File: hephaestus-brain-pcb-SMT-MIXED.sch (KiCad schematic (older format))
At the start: 32 parts, among them IC1 ATSAMD51G19A-MU, J1 Barrel_Jack, J2 Conn_02x03_Odd_Even, J3 USB_B_Micro, J4 Conn_02x10_Odd_Even, J5 Conn_01x03_Male, J6 Conn_01x03_Male, J7 Conn_01x03_Male, SW1 SW_SPDT, SW2 SW_SPST, SW3 SW_SPST, U1 LM1117-5.0, U2 AP2112K-3.3, U3 AT25xxx-MA, U4 74LVC1G125

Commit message: Mixed SMT-PTH version.
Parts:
- J1: footprint unified:DC-005-5A-2.0-SMT -> Connector_BarrelJack:BarrelJack_CUI_PJ-102AH_Horizontal
- J2: footprint Connector_PinSocket_2.54mm:PinSocket_2x03_P2.54mm_Vertical_SMD -> Connector_PinSocket_2.54mm:PinSocket_2x03_P2.54mm_Vertical
- J5, J6, J7: footprint Connector_JST:JST_PH_B3B-PH-SM4-TB_1x03-1MP_P2.00mm_Vertical -> Connector_JST:JST_PH_B3B-PH-K_1x03_P2.00mm_Vertical
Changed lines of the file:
@@
 F 0 "J5" H 4922 4082 50  0000 R CNN
 F 1 "Conn_01x03_Male" H 4922 4173 50  0000 R CNN
-F 2 "Connector_JST:JST_PH_B3B-PH-SM4-TB_1x03-1MP_P2.00mm_Vertical" H 4950 4150 50  0001 C CNN
+F 2 "Connector_JST:JST_PH_B3B-PH-K_1x03_P2.00mm_Vertical" H 4950 4150 50  0001 C CNN
 F 3 "B3B-PH-K-S(LF)(SN)" H 4950 4150 50  0001 C CNN
 	1    4950 4150
@@
 F 0 "J1" H 1457 1975 50  0000 C CNN
 F 1 "Barrel_Jack" H 1457 1884 50  0000 C CNN
-F 2 "unified:DC-005-5A-2.0-SMT" H 1450 1610 50  0001 C CNN
+F 2 "Connector_BarrelJack:BarrelJack_CUI_PJ-102AH_Horizontal" H 1450 1610 50  0001 C CNN
 F 3 "PJ-102AH" H 1450 1610 50  0001 C CNN
 F 4 "DC-005-5A-2.0-SMT" H 1400 1650 50  0001 C CNN "mpn"
@@
 F 0 "J6" H 4922 4432 50  0000 R CNN
 F 1 "Conn_01x03_Male" H 4922 4523 50  0000 R CNN
-F 2 "Connector_JST:JST_PH_B3B-PH-SM4-TB_1x03-1MP_P2.00mm_Vertical" H 4950 4500 50  0001 C CNN
+F 2 "Connector_JST:JST_PH_B3B-PH-K_1x03_P2.00mm_Vertical" H 4950 4500 50  0001 C CNN
 F 3 "B3B-PH-K-S(LF)(SN)" H 4950 4500 50  0001 C CNN
 	1    4950 4500
@@
 F 0 "J7" H 4922 4782 50  0000 R CNN
 F 1 "Conn_01x03_Male" H 4922 4873 50  0000 R CNN
-F 2 "Connector_JST:JST_PH_B3B-PH-SM4-TB_1x03-1MP_P2.00mm_Vertical" H 4950 4850 50  0001 C CNN
+F 2 "Connector_JST:JST_PH_B3B-PH-K_1x03_P2.00mm_Vertical" H 4950 4850 50  0001 C CNN
 F 3 "B3B-PH-K-S(LF)(SN)" H 4950 4850 50  0001 C CNN
 	1    4950 4850
@@
 F 0 "J2" H 5350 3417 50  0000 C CNN
 F 1 "Conn_02x03_Odd_Even" H 5350 3326 50  0000 C CNN
-F 2 "Connector_PinSocket_2.54mm:PinSocket_2x03_P2.54mm_Vertical_SMD" H 5300 3100 50  0001 C CNN
+F 2 "Connector_PinSocket_2.54mm:PinSocket_2x03_P2.54mm_Vertical" H 5300 3100 50  0001 C CNN
 F 3 "~" H 5300 3100 50  0001 C CNN
 	1    5300 3100

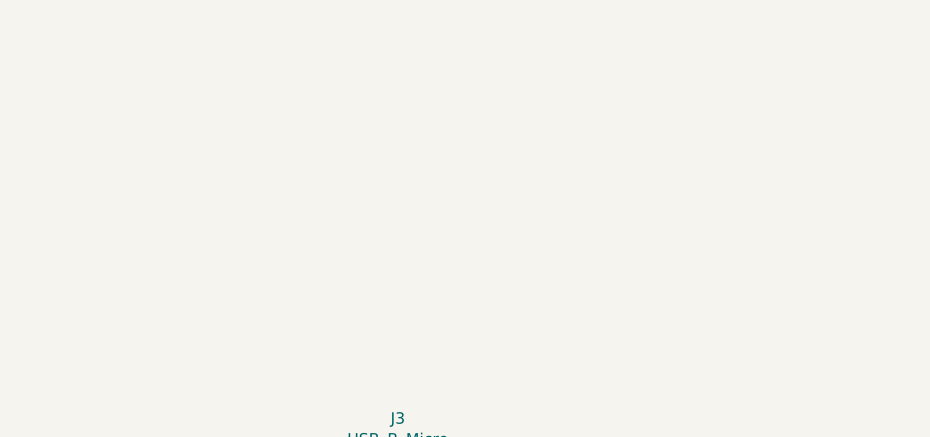
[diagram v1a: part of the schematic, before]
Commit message: Switched over to USBC connector.
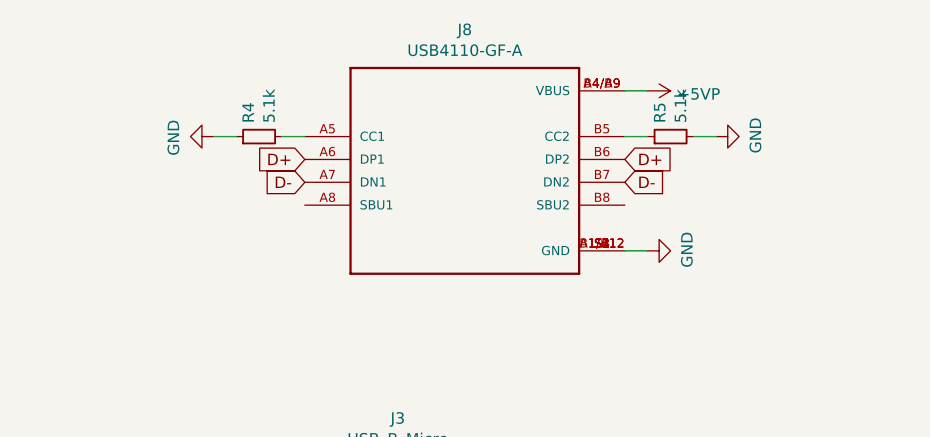
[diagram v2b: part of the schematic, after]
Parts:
- added J8: USB4110-GF-A, unified:GCT_USB4110-GF-A, symbol USB4110-GF-A:USB4110-GF-A
- added R4, R5: 5.1k, Resistor_SMD:R_0603_1608Metric, symbol Device:R_Small
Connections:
- net +5VP: now also J8.A4/B9 (VBUS), J8.B4/A9 (VBUS)
- net D+: now also J8.A6 (DP1), J8.B6 (DP2)
- net D-: now also J8.A7 (DN1), J8.B7 (DN2)
- net GND: now also J8.A1/B12 (GND), J8.B1/A12 (GND), J8.S1 (GND), J8.S2 (GND), J8.S3 (GND), J8.S4 (GND), R4.1, R5.2
- new net: J8.A5 (CC1), R4.2
- new net: J8.B5 (CC2), R5.1
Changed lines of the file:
@@
 Text GLabel 12700 3850 0    50   Input ~ 0
 SWCLK
+$Comp
+L USB4110-GF-A:USB4110-GF-A J8
+U 1 1 5FAEF4FA
+P 9550 -600
+F 0 "J8" H 9550 -33 50  0000 C CNN
+F 1 "USB4110-GF-A" H 9550 -124 50  0000 C CNN
+F 2 "unified:GCT_USB4110-GF-A" H 9550 -600 50  0001 L BNN
+F 3 "3.26 mm" H 9550 -600 50  0001 L BNN
+F 4 "A" H 9550 -600 50  0001 L BNN "Field4"
+F 5 "GCT" H 9550 -600 50  0001 L BNN "Field5"
+F 6 "Manufacturer Recommendations" H 9550 -600 50  0001 L BNN "Field6"
+	1    9550 -600
+	1    0    0    -1
+$EndComp
+Text GLabel 8850 -600 0    50   Input ~ 0
+D+
+Text GLabel 10250 -600 2    50   Input ~ 0
+D+
+Text GLabel 10250 -500 2    50   Input ~ 0
+D-
+Text GLabel 8850 -500 0    50   Input ~ 0
+D-
+$Comp
+L Device:R_Small R5
+U 1 1 5FAF0FFD
+P 10450 -700
+F 0 "R5" H 10509 -654 50  0000 L CNN
+F 1 "5.1k" H 10509 -745 50  0000 L CNN
+F 2 "Resistor_SMD:R_0603_1608Metric" H 10450 -700 50  0001 C CNN
+F 3 "~" H 10450 -700 50  0001 C CNN
+	1    10450 -700
+	0    -1   -1   0
+$EndComp
+$Comp
+L Device:R_Small R4
+U 1 1 5FAF1F44
+P 8650 -700
+F 0 "R4" H 8709 -654 50  0000 L CNN
+F 1 "5.1k" H 8709 -745 50  0000 L CNN
+F 2 "Resistor_SMD:R_0603_1608Metric" H 8650 -700 50  0001 C CNN
+F 3 "~" H 8650 -700 50  0001 C CNN
+	1    8650 -700
+	0    -1   -1   0
+$EndComp
+$Comp
+L power:GND #PWR0138
+U 1 1 5FAF28B7
+P 8450 -700
+F 0 "#PWR0138" H 8450 -950 50  0001 C CNN
+F 1 "GND" H 8455 -873 50  0000 C CNN
+F 2 "" H 8450 -700 50  0001 C CNN
+F 3 "" H 8450 -700 50  0001 C CNN
+	1    8450 -700
+	0    1    1    0
+$EndComp
+$Comp
+L power:GND #PWR0139
+U 1 1 5FAF2FB3
+P 10650 -700
+F 0 "#PWR0139" H 10650 -950 50  0001 C CNN
+F 1 "GND" H 10655 -873 50  0000 C CNN
+F 2 "" H 10650 -700 50  0001 C CNN
+F 3 "" H 10650 -700 50  0001 C CNN
+	1    10650 -700
+	0    -1   -1   0
+$EndComp
+$Comp
+L power:GND #PWR0140
+U 1 1 5FAF3881
+P 10350 -200
+F 0 "#PWR0140" H 10350 -450 50  0001 C CNN
+F 1 "GND" H 10355 -373 50  0000 C CNN
+F 2 "" H 10350 -200 50  0001 C CNN
+F 3 "" H 10350 -200 50  0001 C CNN
+	1    10350 -200
+	0    -1   -1   0
+$EndComp
+Wire Wire Line
+	10350 -700 10250 -700
+Wire Wire Line
+	10650 -700 10550 -700
+Wire Wire Line
+	8850 -700 8750 -700
+Wire Wire Line
+	8550 -700 8450 -700
+Wire Wire Line
+	10350 -200 10250 -200
+$Comp
+L power:+5VP #PWR0141
+U 1 1 5FAFF597
+P 10350 -900
+F 0 "#PWR0141" H 10350 -1050 50  0001 C CNN
+F 1 "+5VP" V 10365 -772 50  0000 L CNN
+F 2 "" H 10350 -900 50  0001 C CNN
+F 3 "" H 10350 -900 50  0001 C CNN
+	1    10350 -900
+	0    1    1    0
+$EndComp
+Wire Wire Line
+	10350 -900 10250 -900
 $EndSCHEMATC

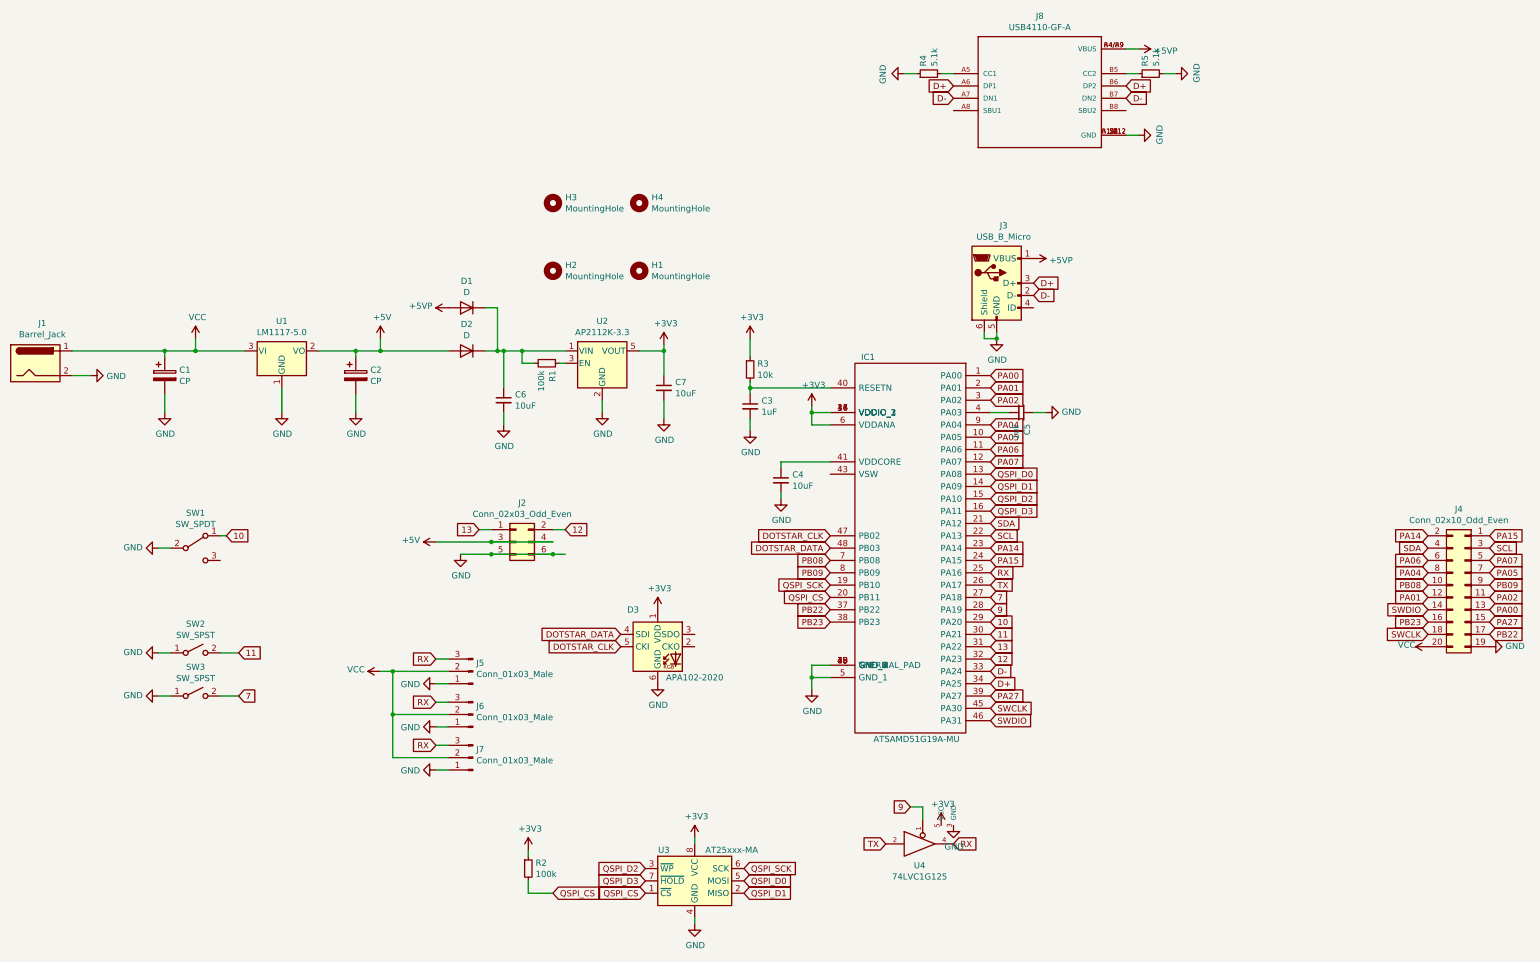
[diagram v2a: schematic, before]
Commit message: Added SWD Connector and QWIIC
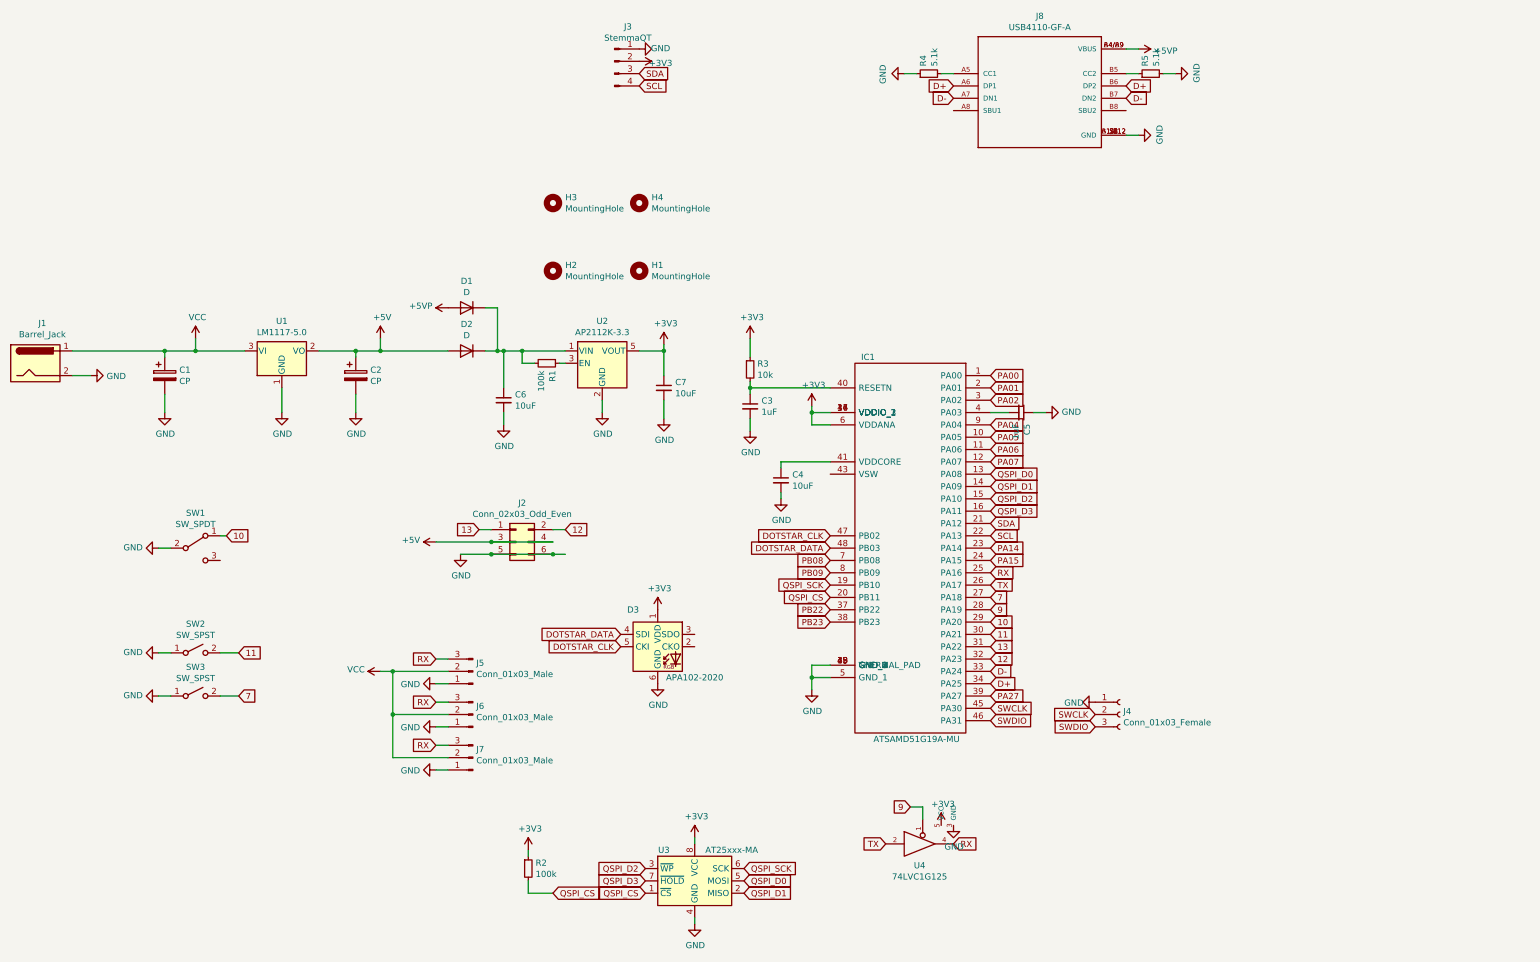
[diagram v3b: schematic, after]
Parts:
- removed J3: USB_B_Micro, Connector_USB:USB_Micro-B_Molex_47346-0001, symbol Connector:USB_B_Micro
- removed J4: Conn_02x10_Odd_Even, Connector_PinSocket_2.54mm:PinSocket_2x10_P2.54mm_Vertical, symbol Connector_Generic:Conn_02x10_Odd_Even
- added J3: StemmaQT, Connector_JST:JST_SH_SM04B-SRSS-TB_1x04-1MP_P1.00mm_Horizontal, symbol Connector:Conn_01x04_Male
- added J4: Conn_01x03_Female, Connector_PinSocket_2.54mm:PinSocket_1x03_P2.54mm_Vertical, symbol Connector:Conn_01x03_Female
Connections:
- net +3V3: now also J3.2 (Pin_2)
- net GND: now also J3.1 (Pin_1), J4.1 (Pin_1)
- net SCL: now also J3.4 (Pin_4)
- net SDA: now also J3.3 (Pin_3)
- net SWCLK: now also J4.2 (Pin_2)
- net SWDIO: now also J4.3 (Pin_3)
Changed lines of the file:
@@
 Wire Wire Line
 	6500 1550 6500 1500
-$Comp
-L Connector:USB_B_Micro J3
-U 1 1 5FA9715B
-P 9200 1000
-F 0 "J3" H 9257 1467 50  0000 C CNN
-F 1 "USB_B_Micro" H 9257 1376 50  0000 C CNN
-F 2 "Connector_USB:USB_Micro-B_Molex_47346-0001" H 9350 950 50  0001 C CNN
-F 3 "~" H 9350 950 50  0001 C CNN
-	1    9200 1000
-	1    0    0    -1
-$EndComp
-Wire Wire Line
-	9100 1400 9100 1450
-Wire Wire Line
-	9200 1400 9200 1450
-Wire Wire Line
-	9200 1450 9100 1450
 Wire Wire Line
 	5050 1550 5150 1550
@@
 	0    -1   -1   0
 $EndComp
-$Comp
-L power:+5VP #PWR0132
-U 1 1 5FAB03EB
-P 9500 800
-F 0 "#PWR0132" H 9500 650 50  0001 C CNN
-F 1 "+5VP" V 9515 928 50  0000 L CNN
-F 2 "" H 9500 800 50  0001 C CNN
-F 3 "" H 9500 800 50  0001 C CNN
-	1    9500 800
-	0    1    1    0
-$EndComp
 Text GLabel 9150 4150 2    50   Input ~ 0
 D-
 Text GLabel 9150 4250 2    50   Input ~ 0
 D+
-Text GLabel 9500 1000 2    50   Input ~ 0
-D+
-Text GLabel 9500 1100 2    50   Input ~ 0
-D-
 $Comp
 L Device:C_Small C6
@@
 	0    1    1    0
 $EndComp
-$Comp
-L power:GND #PWR0119
-U 1 1 5FAE29FD
-P 9200 1450
-F 0 "#PWR0119" H 9200 1200 50  0001 C CNN
-F 1 "GND" H 9205 1277 50  0000 C CNN
-F 2 "" H 9200 1450 50  0001 C CNN
-F 3 "" H 9200 1450 50  0001 C CNN
-	1    9200 1450
-	1    0    0    -1
-$EndComp
-Connection ~ 9200 1450
 Wire Wire Line
 	2700 1550 3100 1550
@@
 Text GLabel 3050 4350 2    50   Input ~ 0
 7
-$Comp
-L Connector_Generic:Conn_02x10_Odd_Even J4
-U 1 1 5FBE64F5
-P 13000 3450
-F 0 "J4" H 13050 4067 50  0000 C CNN
-F 1 "Conn_02x10_Odd_Even" H 13050 3976 50  0000 C CNN
-F 2 "Connector_PinSocket_2.54mm:PinSocket_2x10_P2.54mm_Vertical" H 13000 3450 50  0001 C CNN
-F 3 "~" H 13000 3450 50  0001 C CNN
-	1    13000 3450
-	-1   0    0    -1
-$EndComp
 Text GLabel 9150 3250 2    50   Input ~ 0
-PA15
-Text GLabel 13200 3050 2    50   Input ~ 0
 PA15
 Text GLabel 9150 3150 2    50   Input ~ 0
 PA14
-Text GLabel 12700 3050 0    50   Input ~ 0
-PA14
-Text GLabel 13200 3150 2    50   Input ~ 0
-SCL
-Text GLabel 12700 3150 0    50   Input ~ 0
-SDA
 Text GLabel 9150 4350 2    50   Input ~ 0
 PA27
@@
 Text GLabel 7850 3750 0    50   Input ~ 0
 PB23
-Text GLabel 13200 3250 2    50   Input ~ 0
-PA07
-Text GLabel 13200 3350 2    50   Input ~ 0
-PA05
-Text GLabel 13200 3450 2    50   Input ~ 0
-PB09
-Text GLabel 13200 3550 2    50   Input ~ 0
-PA02
-Text GLabel 13200 3650 2    50   Input ~ 0
-PA00
-Text GLabel 13200 3750 2    50   Input ~ 0
-PA27
-Text GLabel 13200 3850 2    50   Input ~ 0
-PB22
-Text GLabel 12700 3750 0    50   Input ~ 0
-PB23
-Text GLabel 12700 3650 0    50   Input ~ 0
-SWDIO
-Text GLabel 12700 3550 0    50   Input ~ 0
-PA01
-Text GLabel 12700 3450 0    50   Input ~ 0
-PB08
-Text GLabel 12700 3350 0    50   Input ~ 0
-PA04
-Text GLabel 12700 3250 0    50   Input ~ 0
-PA06
-$Comp
-L power:GND #PWR0136
-U 1 1 5FBF8572
-P 13200 3950
-F 0 "#PWR0136" H 13200 3700 50  0001 C CNN
-F 1 "GND" V 13205 3822 50  0000 R CNN
-F 2 "" H 13200 3950 50  0001 C CNN
-F 3 "" H 13200 3950 50  0001 C CNN
-	1    13200 3950
-	0    -1   -1   0
-$EndComp
-$Comp
-L power:VCC #PWR0137
-U 1 1 5FBF92B7
-P 12700 3950
-F 0 "#PWR0137" H 12700 3800 50  0001 C CNN
-F 1 "VCC" V 12715 4123 50  0000 C CNN
-F 2 "" H 12700 3950 50  0001 C CNN
-F 3 "" H 12700 3950 50  0001 C CNN
-	1    12700 3950
-	0    -1   -1   0
-$EndComp
-Text GLabel 12700 3850 0    50   Input ~ 0
-SWCLK
 $Comp
 L USB4110-GF-A:USB4110-GF-A J8
@@
 Wire Wire Line
 	10350 -900 10250 -900
+$Comp
+L Connector:Conn_01x04_Male J3
+U 1 1 5FAF1AFD
+P 6100 -800
+F 0 "J3" H 6208 -519 50  0000 C CNN
+F 1 "StemmaQT" H 6208 -610 50  0000 C CNN
+F 2 "Connector_JST:JST_SH_SM04B-SRSS-TB_1x04-1MP_P1.00mm_Horizontal" H 6100 -800 50  0001 C CNN
+F 3 "~" H 6100 -800 50  0001 C CNN
+	1    6100 -800
+	1    0    0    -1
+$EndComp
+$Comp
+L power:GND #PWR0119
+U 1 1 5FAF284B
+P 6300 -900
+F 0 "#PWR0119" H 6300 -1150 50  0001 C CNN
+F 1 "GND" V 6305 -1073 50  0000 C CNN
+F 2 "" H 6300 -900 50  0001 C CNN
+F 3 "" H 6300 -900 50  0001 C CNN
+	1    6300 -900
+	0    -1   -1   0
+$EndComp
+$Comp
+L power:+3V3 #PWR0132
+U 1 1 5FAF2D41
+P 6300 -800
+F 0 "#PWR0132" H 6300 -950 50  0001 C CNN
+F 1 "+3V3" V 6315 -627 50  0000 C CNN
+F 2 "" H 6300 -800 50  0001 C CNN
+F 3 "" H 6300 -800 50  0001 C CNN
+	1    6300 -800
+	0    1    1    0
+$EndComp
+Text GLabel 6300 -700 2    50   Input ~ 0
+SDA
+Text GLabel 6300 -600 2    50   Input ~ 0
+SCL
+$Comp
+L Connector:Conn_01x03_Female J4
+U 1 1 5FAF396B
+P 10200 4500
+F 0 "J4" H 10228 4526 50  0000 L CNN
+F 1 "Conn_01x03_Female" H 10228 4435 50  0000 L CNN
+F 2 "Connector_PinSocket_2.54mm:PinSocket_1x03_P2.54mm_Vertical" H 10200 4500 50  0001 C CNN
+F 3 "~" H 10200 4500 50  0001 C CNN
+	1    10200 4500
+	1    0    0    -1
+$EndComp
+$Comp
+L power:GND #PWR0136
+U 1 1 5FAF49CA
+P 10000 4400
+F 0 "#PWR0136" H 10000 4150 50  0001 C CNN
+F 1 "GND" V 10005 4227 50  0000 C CNN
+F 2 "" H 10000 4400 50  0001 C CNN
+F 3 "" H 10000 4400 50  0001 C CNN
+	1    10000 4400
+	0    1    1    0
+$EndComp
+Text GLabel 10000 4600 0    50   Input ~ 0
+SWDIO
+Text GLabel 10000 4500 0    50   Input ~ 0
+SWCLK
 $EndSCHEMATC
